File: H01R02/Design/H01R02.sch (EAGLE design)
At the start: 31 parts, among them P1 HEXABIT_17.32, Q1 MMBT3904LT1, Q2 MMBT3904LT1, Q3 MMBT3904LT1, X1 XTALL_CSTCE8M00G52

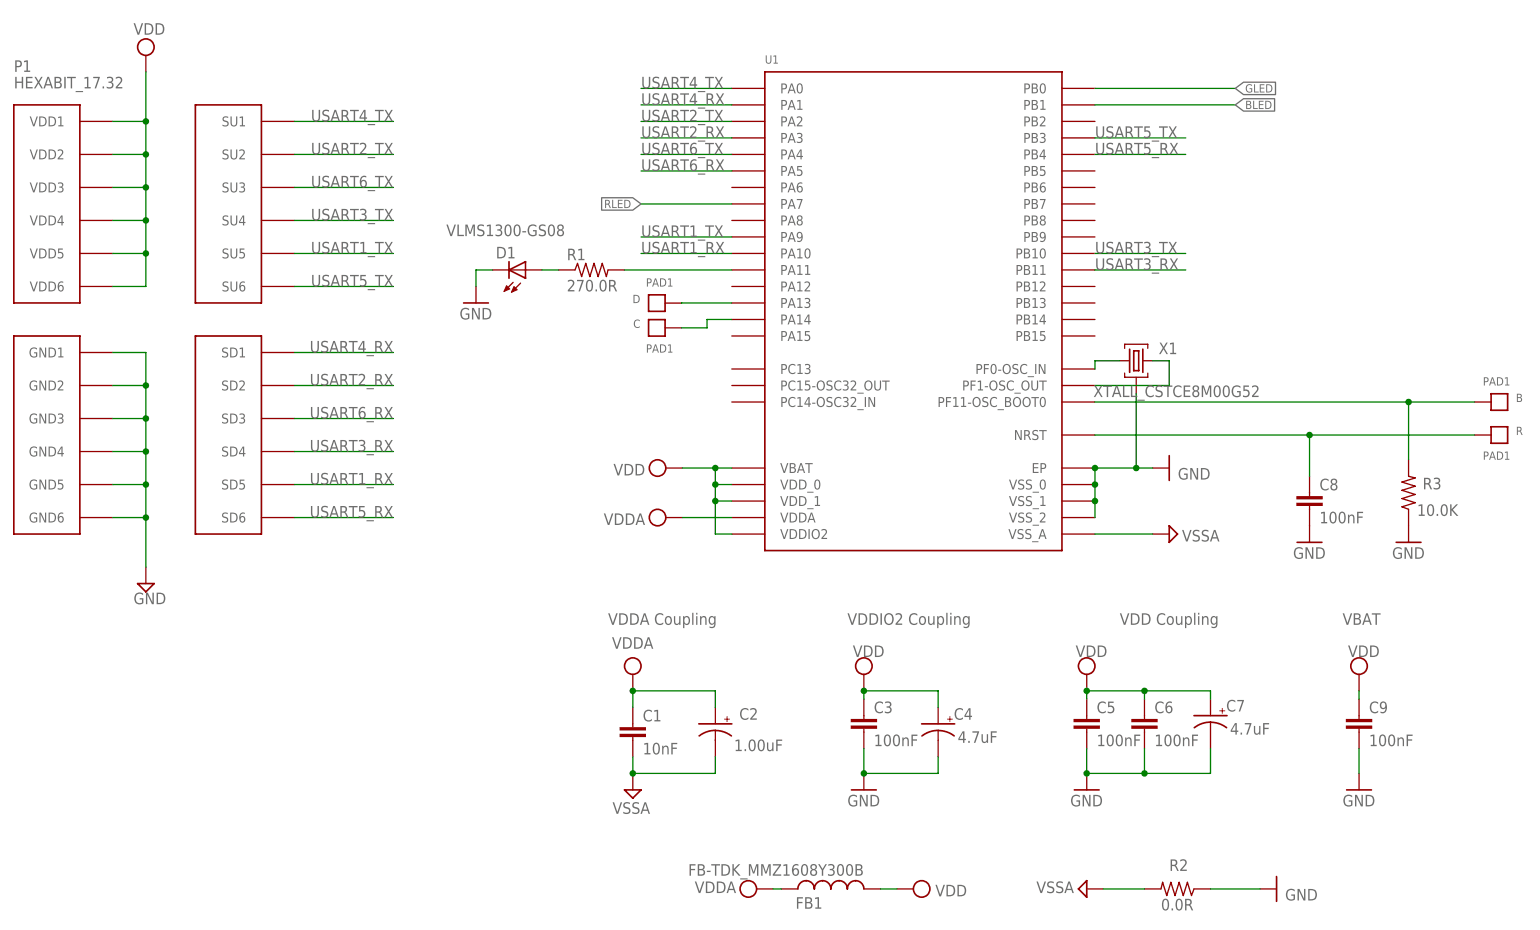
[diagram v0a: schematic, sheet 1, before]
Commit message: Changing MCU to STM32G0
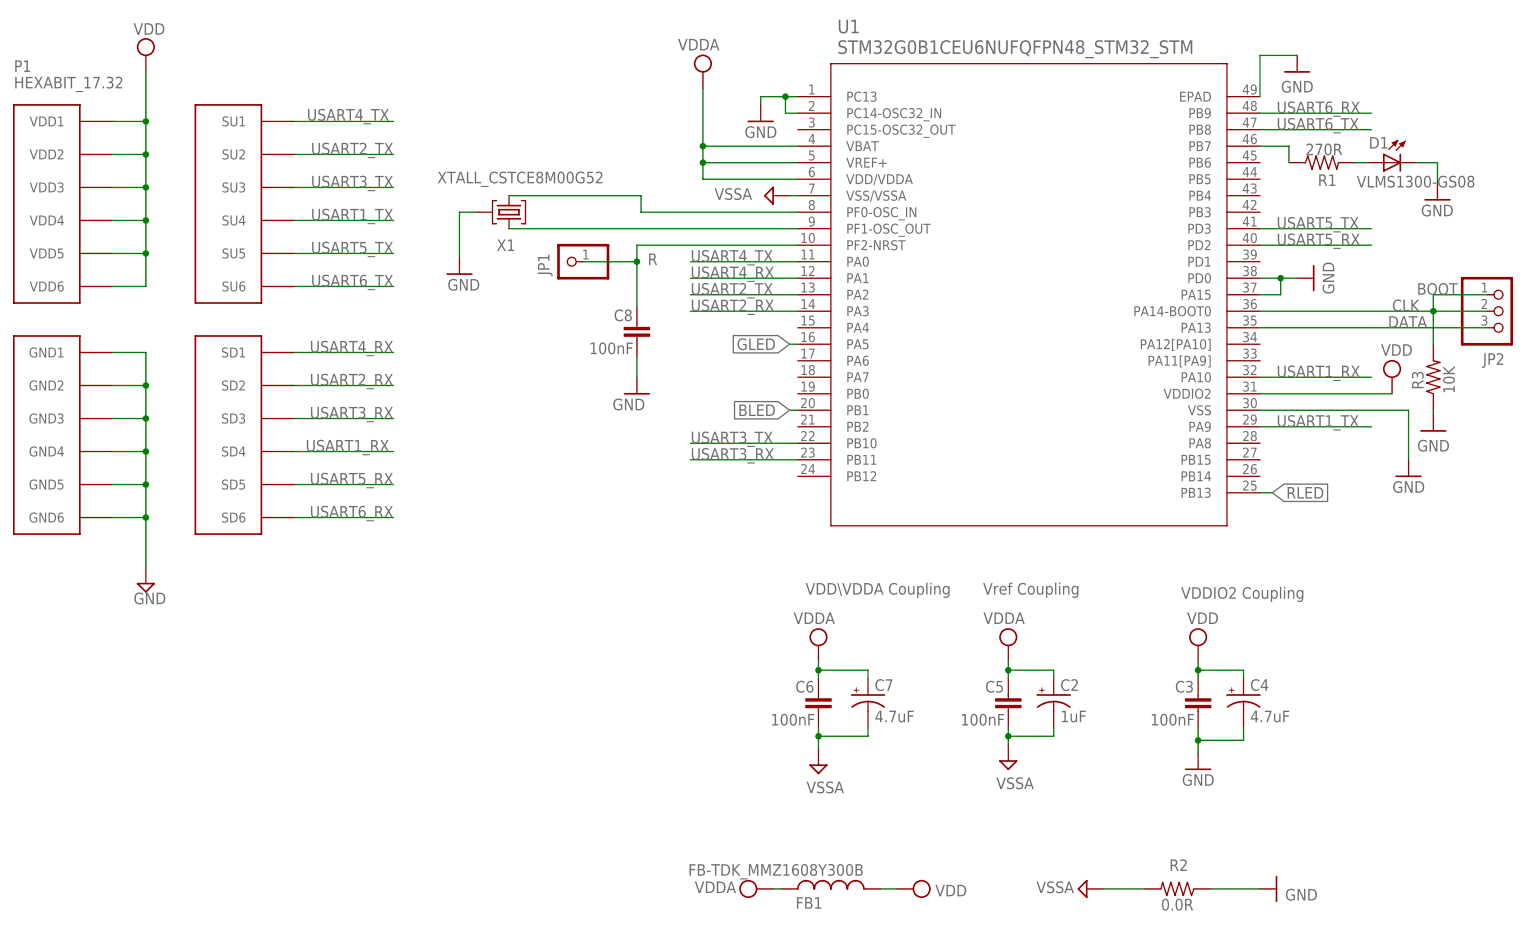
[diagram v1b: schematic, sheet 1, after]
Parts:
- removed B, C, D, R: PAD1, Hexabitz:PAD1
- removed C1: 10nF, Hexabitz:C-0603
- removed C9: 100nF, Hexabitz:C-0603
- added JP1: R, HEXABITZ_USER_INTERFACE_PARTS:PINHD-1X1
- added JP2: (no value), pinhead:PINHD-1X3
- C2: value 1.00uF -> 1uF; device Hexabitz:C-0805-POL -> HEXABITZ_RCLS:C-0805-POL; CAPACITANCE 1.00uF -> (none); MFN Yageo -> (none); MPN CC0805KKX7R7BB105 -> (none); OCTOPART_URL https://octopart.com/cc0805kkx7r7bb105-yageo-8376555?r=sp&s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 -> (none); TOLERANCE 10% -> (none); VOLTAGE_RATING 16V -> (none)
- C3, C6, C8: device Hexabitz:C-0603 -> HEXABITZ_RCLS:C-0603; CAPACITANCE 100nF -> (none); MFN KEMET -> (none); MPN C0603C104K8RACTU -> (none); OCTOPART_URL https://octopart.com/c0603c104k8ractu-kemet-145075?r=sp&s=9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 -> (none); TOLERANCE 10% -> (none); VOLTAGE_RATING 10V -> (none)
- C4, C7: device Hexabitz:C-0805-POL -> HEXABITZ_RCLS:C-0805-POL; CAPACITANCE 4.7uF -> (none); MFN Murata -> (none); MPN GRM21BC81E475KA12L -> (none); OCTOPART_URL https://octopart.com/grm21bc81e475ka12l-murata-10331911?r=s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 -> (none); TOLERANCE 10% -> (none); VOLTAGE_RATING 25V -> (none)
- C5: device Hexabitz:C-0603 -> HEXABITZ_RCLS:C-0603; CAPACITANCE 100nF -> (none); MFN KEMET -> (none); MPN C0603C104K8RACTU -> (none); OCTOPART_URL https://octopart.com/c0603c104k8ractu-kemet-145075?r=sp&s=9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 -> (none); TOLERANCE 10% -> (none); VOLTAGE_RATING 10 -> (none)
- FB1: device Hexabitz:FB-TDK_MMZ1608Y300B -> HEXABITZ_RCLS:FB-TDK_MMZ1608Y300B
- Q1, Q2, Q3: device Hexabitz:MMBT3904LT1 -> HEXABITZ_RCLS:MMBT3904LT1
- R1: value 270.0R -> 270R; device Hexabitz:R-0603 -> HEXABITZ_RCLS:R-0603; MFN Yageo -> (none); MPN RC0603FR-07270RL -> (none); OCTOPART_URL https://octopart.com/search?q=RC0603FR-07270RL&start=0 -> (none); RESISTANCE 270.0 Ohm -> (none); TOLERANCE 5% -> (none)
- R2, R4, R5, R6, R7, R8, R9: device Hexabitz:R-0603 -> HEXABITZ_RCLS:R-0603
- R3: value 10.0K -> 10K; device Hexabitz:R-0603 -> HEXABITZ_RCLS:R-0603; MFN Yageo -> (none); MPN RC0603JR-0710KL -> (none); OCTOPART_URL https://octopart.com/search?q=RC0603JR-0710KL&start=0 -> (none); RESISTANCE 10.0K Ohm -> (none); TOLERANCE 5% -> (none)
- U1: value (none) -> STM32G0B1CEU6NUFQFPN48_STM32_STM; device Hexabitz:STM32F091CBU6 -> HEXABITZ_ICs:STM32G0B1CEU6NUFQFPN48_STM32_STM
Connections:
- removed net B1: B.P$1, R3.2, U1.PF11-OSC_BOOT0
- removed net N$9: C.P$1, U1.PA14
- removed net R1: C8.1, R.P$1, U1.NRST
- new net CLK: JP2.1, JP2.2, R3.2, U1.PA14-BOOT0
- new net DATA: JP2.3, U1.PA13
- net GLED: now also U1.PA5; no longer U1.PB0
- net GND: now also U1.EPAD, U1.PA15, U1.PC13, U1.PC14-OSC32_IN, U1.PD0, U1.VSS; no longer C5.2, C6.2, C7.-, C9.2, U1.EP, U1.VSS_0, U1.VSS_1, U1.VSS_2
- net N$3: now also D1.A; no longer U1.PA11
- net N$4: now also C8.1, JP1.1, U1.PF2-NRST; no longer D1.A, R1.1
- net N$5: now also U1.PF1-OSC_OUT; no longer U1.PF0-OSC_IN
- net N$6: now also U1.PF0-OSC_IN; no longer U1.PF1-OSC_OUT
- net N$7: now also R1.1, U1.PB7; no longer D.P$1, U1.PA13
- net RLED: now also U1.PB13; no longer U1.PA7
- net USART1_RX: now also P1.SD4; no longer P1.SD5
- net USART1_TX: now also P1.SU4; no longer P1.SU5
- net USART3_RX: now also P1.SD3; no longer P1.SD4
- net USART3_TX: now also P1.SU3; no longer P1.SU4
- net USART5_RX: now also P1.SD5, U1.PD2; no longer P1.SD6, U1.PB4
- net USART5_TX: now also P1.SU5, U1.PD3; no longer P1.SU6, U1.PB3
- net USART6_RX: now also P1.SD6, U1.PB9; no longer P1.SD3, U1.PA5
- net USART6_TX: now also P1.SU6, U1.PB8; no longer P1.SU3, U1.PA4
- net VDD: no longer C5.1, C6.1, C7.+, C9.1, U1.VBAT, U1.VDD_0, U1.VDD_1
- net VDDA: now also C5.1, C6.1, C7.+, U1.VBAT, U1.VDD/VDDA, U1.VREF+; no longer C1.1, U1.VDDA
- net VSSA: now also C5.2, C6.2, C7.-, U1.VSS/VSSA; no longer C1.2, U1.VSS_A
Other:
- note added: "BOOT"
- note added: "H01R02"
- note added: "H01R02_Backend"
- note added: "H01R02_Frontend"
- note added: "Obada Albasha"
- note added: "VDD\VDDA Coupling"
- note added: "Vref Coupling"
- note removed: "Anas Kaadan"
- note removed: "H01R0"
- note removed: "H01R0_Frontend"
- note removed: "VBAT"
- note removed: "VDD Coupling"
- note removed: "VDDA Coupling"
- moved on the sheet: C2, C3, C4, C5, C6, C7, C8, D1, R1, R3, X1
